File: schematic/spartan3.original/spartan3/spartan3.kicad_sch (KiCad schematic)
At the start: 206 parts, among them U1_clk_select_0 SPFT_Sliding_Switch-dynacore, U2 XC3S250E-4TQG144C

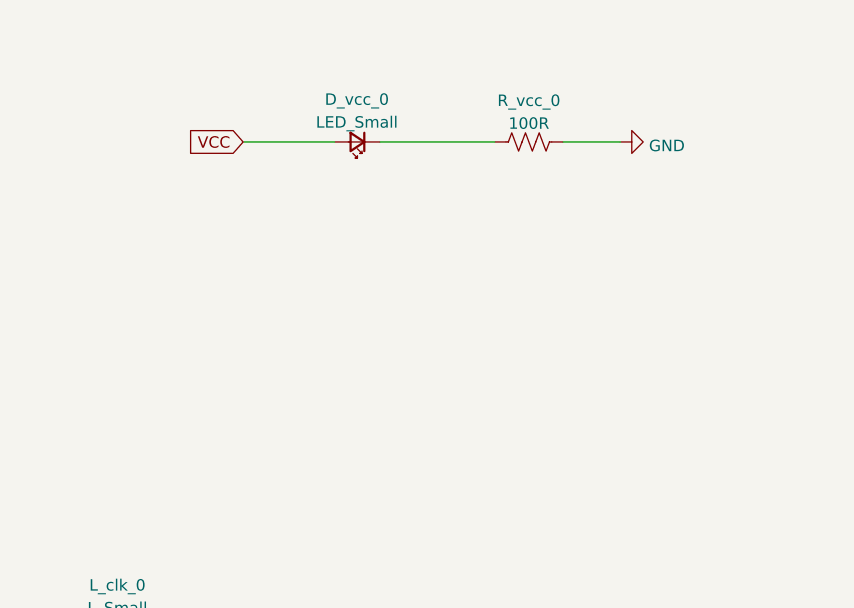
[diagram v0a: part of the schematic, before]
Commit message: Schematics :: reset added
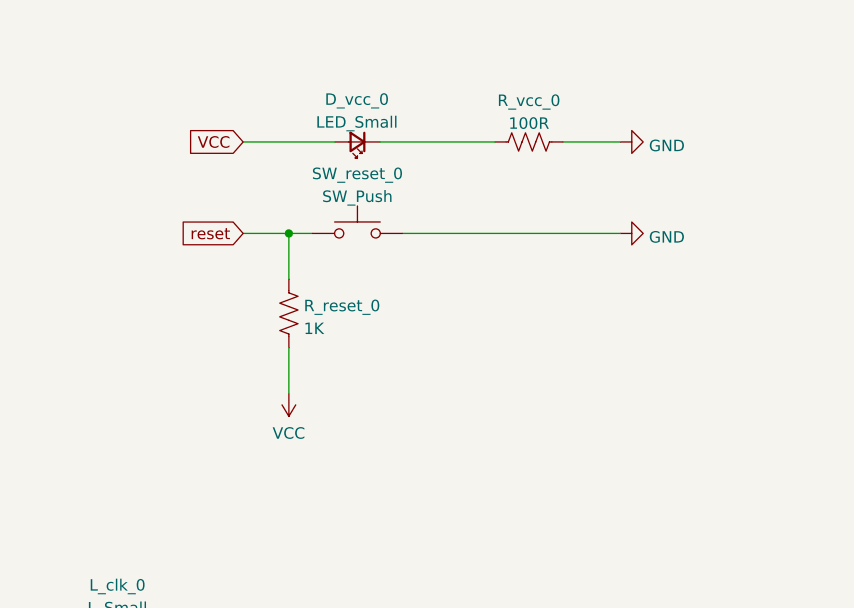
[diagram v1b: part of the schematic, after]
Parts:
- added R_reset_0: 1K, Resistor_SMD:R_0805_2012Metric_Pad1.20x1.40mm_HandSolder, symbol Device:R_US
- added SW_reset_0: SW_Push, Button_Switch_THT:SW_PUSH_6mm_H9.5mm, symbol Switch:SW_Push
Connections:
- net GND: now also SW_reset_0.2
- net VCC: now also R_reset_0.1
- new net reset: R_reset_0.2, SW_reset_0.1
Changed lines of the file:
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@@
   (junction (at 412.75 406.4) (diameter 0) (color 0 0 0 0)
   )
+  (junction (at 850.9 248.92) (diameter 0) (color 0 0 0 0)
+  )
   (junction (at 685.8 177.8) (diameter 0) (color 0 0 0 0)
   )
@@
     (stroke (width 0) (type default) (color 0 0 0 0))
   )
+  (wire (pts (xy 845.82 248.92) (xy 850.9 248.92))
+    (stroke (width 0) (type default) (color 0 0 0 0))
+  )
   (wire (pts (xy 412.75 298.45) (xy 412.75 299.72))
     (stroke (width 0) (type default) (color 0 0 0 0))
@@
     (stroke (width 0) (type default) (color 0 0 0 0))
   )
+  (wire (pts (xy 850.9 248.92) (xy 850.9 254))
+    (stroke (width 0) (type default) (color 0 0 0 0))
+  )
   (wire (pts (xy 317.5 297.18) (xy 317.5 298.45))
     (stroke (width 0) (type default) (color 0 0 0 0))
@@
     (stroke (width 0) (type default) (color 0 0 0 0))
   )
+  (wire (pts (xy 850.9 248.92) (xy 853.44 248.92))
+    (stroke (width 0) (type default) (color 0 0 0 0))
+  )
   (wire (pts (xy 901.7 309.88) (xy 914.4 309.88))
     (stroke (width 0) (type default) (color 0 0 0 0))
@@
     (stroke (width 0) (type default) (color 0 0 0 0))
   )
+  (wire (pts (xy 863.6 248.92) (xy 887.73 248.92))
+    (stroke (width 0) (type default) (color 0 0 0 0))
+  )
   (wire (pts (xy 129.54 215.9) (xy 139.7 215.9))
     (stroke (width 0) (type default) (color 0 0 0 0))
@@
     (stroke (width 0) (type default) (color 0 0 0 0))
   )
+  (wire (pts (xy 850.9 261.62) (xy 850.9 266.7))
+    (stroke (width 0) (type default) (color 0 0 0 0))
+  )
   (wire (pts (xy 508 50.8) (xy 514.35 50.8))
     (stroke (width 0) (type default) (color 0 0 0 0))
@@
     )
   )
+  (global_label "reset" (shape input) (at 845.82 248.92 180) (fields_autoplaced)
+    (effects (font (size 1.27 1.27)) (justify right))
+    (property "Intersheet References" "${INTERSHEET_REFS}" (id 0) (at 838.6898 248.8406 0)
+      (effects (font (size 1.27 1.27)) (justify right) hide)
+    )
+  )
   (global_label "in_ram_w" (shape input) (at 675.64 330.2 180) (fields_autoplaced)
     (effects (font (size 1.27 1.27)) (justify right))
@@
     (pin "1")
   )
+  (symbol (lib_id "Switch:SW_Push") (at 858.52 248.92 0) (unit 1)
+    (in_bom yes) (on_board yes) (fields_autoplaced)
+    (property "Reference" "SW_reset_0" (id 0) (at 858.52 242.2992 0))
+    (property "Value" "SW_Push" (id 1) (at 858.52 244.8361 0))
+    (property "Footprint" "Button_Switch_THT:SW_PUSH_6mm_H9.5mm" (id 2) (at 858.52 243.84 0)
+      (effects (font (size 1.27 1.27)) hide)
+    )
+    (property "Datasheet" "~" (id 3) (at 858.52 243.84 0)
+      (effects (font (size 1.27 1.27)) hide)
+    )
+    (pin "1")
+    (pin "2")
+  )
   (symbol (lib_id "Device:LED_Small") (at 762 173.99 90) (unit 1)
     (in_bom yes) (on_board yes) (fields_autoplaced)
@@
     (pin "1")
   )
+  (symbol (lib_id "power:VCC") (at 850.9 266.7 180) (unit 1)
+    (in_bom yes) (on_board yes) (fields_autoplaced)
+    (property "Reference" "#PWR0252" (id 0) (at 850.9 262.89 0)
+      (effects (font (size 1.27 1.27)) hide)
+    )
+    (property "Value" "VCC" (id 1) (at 850.9 271.1434 0))
+    (property "Footprint" "" (id 2) (at 850.9 266.7 0)
+      (effects (font (size 1.27 1.27)) hide)
+    )
+    (property "Datasheet" "" (id 3) (at 850.9 266.7 0)
+      (effects (font (size 1.27 1.27)) hide)
+    )
+    (pin "1")
+  )
   (symbol (lib_id "power:GND") (at 717.55 213.36 90) (unit 1)
     (in_bom yes) (on_board yes) (fields_autoplaced)
@@
     (pin "2")
   )
+  (symbol (lib_id "power:GND") (at 887.73 248.92 90) (unit 1)
+    (in_bom yes) (on_board yes) (fields_autoplaced)
+    (property "Reference" "#PWR0251" (id 0) (at 894.08 248.92 0)
+      (effects (font (size 1.27 1.27)) hide)
+    )
+    (property "Value" "GND" (id 1) (at 890.905 249.3538 90)
+      (effects (font (size 1.27 1.27)) (justify right))
+    )
+    (property "Footprint" "" (id 2) (at 887.73 248.92 0)
+      (effects (font (size 1.27 1.27)) hide)
+    )
+    (property "Datasheet" "" (id 3) (at 887.73 248.92 0)
+      (effects (font (size 1.27 1.27)) hide)
+    )
+    (pin "1")
+  )
   (symbol (lib_id "power:VCC") (at 514.35 76.2 180) (unit 1)
     (in_bom yes) (on_board yes) (fields_autoplaced)
@@
     (pin "2")
   )
+  (symbol (lib_id "Device:R_US") (at 850.9 257.81 180) (unit 1)
+    (in_bom yes) (on_board yes) (fields_autoplaced)
+    (property "Reference" "R_reset_0" (id 0) (at 852.551 256.9753 0)
+      (effects (font (size 1.27 1.27)) (justify right))
+    )
+    (property "Value" "1K" (id 1) (at 852.551 259.5122 0)
+      (effects (font (size 1.27 1.27)) (justify right))
+    )
+    (property "Footprint" "Resistor_SMD:R_0805_2012Metric_Pad1.20x1.40mm_HandSolder" (id 2) (at 849.884 257.556 90)
+      (effects (font (size 1.27 1.27)) hide)
+    )
+    (property "Datasheet" "~" (id 3) (at 850.9 257.81 0)
+      (effects (font (size 1.27 1.27)) hide)
+    )
+    (pin "1")
+    (pin "2")
+  )
   (symbol (lib_id "Device:R_US") (at 450.85 67.31 0) (unit 1)
     (in_bom yes) (on_board yes) (fields_autoplaced)
@@
       (reference "#PWR0250") (unit 1) (value "GND") (footprint "")
     )
+    (path "/c2e867b7-cc1c-4161-9b5f-6d9bb039bb16"
+      (reference "#PWR0251") (unit 1) (value "GND") (footprint "")
+    )
+    (path "/c1058ec3-aaf6-4e15-be2c-ea2cca1c2665"
+      (reference "#PWR0252") (unit 1) (value "VCC") (footprint "")
+    )
     (path "/25f84511-8044-4092-a57a-275fe021ef47"
       (reference "C_clk_0") (unit 1) (value "0.1uF") (footprint "Capacitor_SMD:C_0805_2012Metric_Pad1.18x1.45mm_HandSolder")
@@
       (reference "R_out_temp_w_0") (unit 1) (value "100R") (footprint "Resistor_SMD:R_0805_2012Metric_Pad1.20x1.40mm_HandSolder")
     )
+    (path "/fc10d999-524c-4ab3-9f2d-33fffce35e4f"
+      (reference "R_reset_0") (unit 1) (value "1K") (footprint "Resistor_SMD:R_0805_2012Metric_Pad1.20x1.40mm_HandSolder")
+    )
     (path "/37f06184-9457-42c5-a75e-4071dfdcb627"
       (reference "R_vcc_0") (unit 1) (value "100R") (footprint "Resistor_SMD:R_0805_2012Metric_Pad1.20x1.40mm_HandSolder")
@@
       (reference "SW_read_register_0") (unit 1) (value "SW_Rotary12") (footprint "SR26 1-1-12P:SR26 1-1-12P")
     )
+    (path "/1682c353-3a8a-416c-8478-fd455b67bc33"
+      (reference "SW_reset_0") (unit 1) (value "SW_Push") (footprint "Button_Switch_THT:SW_PUSH_6mm_H9.5mm")
+    )
     (path "/3dc17902-13b6-4e7e-8b7b-bbfdc1838232"

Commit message: PCB layout :: Implementation process started
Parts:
- D_out_sysbus_0, D_out_sysbus_1, D_out_sysbus_2, D_out_sysbus_3, D_out_sysbus_4, D_out_sysbus_5, D_out_sysbus_6, D_out_sysbus_7: footprint SW_SPDT_small:SW_SPDT_Small -> LED_SMD:LED_0805_2012Metric_Pad1.15x1.40mm_HandSolder
- SW_in_manual_input_o_0, SW_in_manual_input_o_1, SW_in_manual_input_o_2, SW_in_manual_input_o_3, SW_in_manual_input_o_4, SW_in_manual_input_o_5, SW_in_manual_input_o_6, SW_in_manual_input_o_7: footprint Button_Switch_THT:SW_Slide_1P2T_CK_OS102011MS2Q -> SW_SPDT_small:SW_SPDT_Small
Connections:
- net GND: now also U1_clk_select_0.1 (Common), U1_clk_select_0.7 (Common); no longer U1_clk_select_0.~ (P5)
- net in_is_clk_external: now also U1_clk_select_0.3 (P2); no longer U1_clk_select_0.~ (P5)
- net in_is_clk_high: now also U1_clk_select_0.4 (P3); no longer U1_clk_select_0.~ (P5)
- net in_is_clk_low: now also U1_clk_select_0.5 (P4); no longer U1_clk_select_0.~ (P5)
- net in_is_clk_manual: now also U1_clk_select_0.6 (P5); no longer U1_clk_select_0.~ (P5)
- net in_is_clk_veryhigh: now also U1_clk_select_0.2 (P1); no longer U1_clk_select_0.~ (P5)

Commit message: Schematics :: Read Register fixed -- Rs added. PCB layout :: Updated
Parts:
- added D_in_none_r_0: LED_Small, LED_SMD:LED_0805_2012Metric_Pad1.15x1.40mm_HandSolder, symbol Device:LED_Small
- added R_d_in_acc_r_0, R_d_in_iar_r_0, R_d_in_ir_r_0, R_d_in_manual_input_r_0, R_d_in_none_r_0, R_d_in_r0_r_0, R_d_in_r1_r_0, R_d_in_r2_r_0, R_d_in_r3_r_0, R_d_in_ram_r_0: 100R, Resistor_SMD:R_0805_2012Metric_Pad1.20x1.40mm_HandSolder, symbol Device:R_US
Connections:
- net VCC: now also R_d_in_acc_r_0.1, R_d_in_iar_r_0.1, R_d_in_ir_r_0.1, R_d_in_manual_input_r_0.1, R_d_in_none_r_0.1, R_d_in_r0_r_0.1, R_d_in_r1_r_0.1, R_d_in_r2_r_0.1, R_d_in_r3_r_0.1, R_d_in_ram_r_0.1; no longer D_in_acc_r_0.2 (A), D_in_iar_r_0.2 (A), D_in_ir_r_0.2 (A), D_in_manual_input_r_0.2 (A), D_in_r0_r_0.2 (A), D_in_r1_r_0.2 (A), D_in_r2_r_0.2 (A), D_in_r3_r_0.2 (A), D_in_ram_r_0.2 (A)
- net in_acc_r: now also SW_read_register_0.7; no longer SW_read_register_0.3
- net in_iar_r: now also SW_read_register_0.5; no longer SW_read_register_0.1
- net in_ir_r: now also SW_read_register_0.6; no longer SW_read_register_0.2
- net in_manual_input_r: now also SW_read_register_0.1; no longer SW_read_register_0.9
- net in_r0_r: now also SW_read_register_0.9; no longer SW_read_register_0.5
- net in_r1_r: now also SW_read_register_0.10; no longer SW_read_register_0.6
- net in_r2_r: now also SW_read_register_0.11; no longer SW_read_register_0.7
- net in_r3_r: now also SW_read_register_0.12; no longer SW_read_register_0.8
- net in_ram_r: now also SW_read_register_0.8; no longer SW_read_register_0.4
- new net: D_in_none_r_0.1 (K), SW_read_register_0.4
- new net: D_in_manual_input_r_0.2 (A), R_d_in_manual_input_r_0.2
- new net: D_in_iar_r_0.2 (A), R_d_in_iar_r_0.2
- new net: D_in_acc_r_0.2 (A), R_d_in_acc_r_0.2
- new net: D_in_r0_r_0.2 (A), R_d_in_r0_r_0.2
- new net: D_in_r3_r_0.2 (A), R_d_in_r3_r_0.2
- new net: D_in_r1_r_0.2 (A), R_d_in_r1_r_0.2
- new net: D_in_ram_r_0.2 (A), R_d_in_ram_r_0.2
- new net: D_in_r2_r_0.2 (A), R_d_in_r2_r_0.2
- new net: D_in_ir_r_0.2 (A), R_d_in_ir_r_0.2
- new net: D_in_none_r_0.2 (A), R_d_in_none_r_0.2
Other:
- moved on the sheet: D_in_acc_r_0, D_in_iar_r_0, D_in_ir_r_0, D_in_manual_input_r_0, D_in_r0_r_0, D_in_r1_r_0, D_in_r2_r_0, D_in_r3_r_0, D_in_ram_r_0, R_in_acc_r_0, R_in_iar_r_0, R_in_ir_r_0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

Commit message: Schematics :: updated / PCB layout :: updated
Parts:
- added R_d_in_acc_w_0, R_d_in_bus1_one_0, R_d_in_bus1_ps_0, R_d_in_clk_manual_0, R_d_in_iar_w_0, R_d_in_ir_w_0, R_d_in_is_bus1_w_0, R_d_in_is_clk_external_0, R_d_in_is_clk_high_0, R_d_in_is_clk_low_0, R_d_in_is_clk_manual_0, R_d_in_is_clk_veryhigh_0, R_d_in_r0_w_0, R_d_in_r1_w_0, R_d_in_r2_w_0, R_d_in_r3_w_0, R_d_in_ram_a_w_0, R_d_in_ram_w_0, R_d_in_read_reg_en_0, R_d_in_temp_w_0, R_d_in_write_reg_en_0: 100R, Resistor_SMD:R_0805_2012Metric_Pad1.20x1.40mm_HandSolder, symbol Device:R_US
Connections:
- net GND: now also R_d_in_bus1_ps_0.1; no longer D_in_bus1_ps_0.1 (K)
- net VCC: now also R_d_in_acc_w_0.1, R_d_in_bus1_one_0.2, R_d_in_clk_manual_0.1, R_d_in_iar_w_0.1, R_d_in_ir_w_0.1, R_d_in_is_bus1_w_0.1, R_d_in_is_clk_external_0.1, R_d_in_is_clk_high_0.1, R_d_in_is_clk_low_0.1, R_d_in_is_clk_manual_0.1, R_d_in_is_clk_veryhigh_0.1, R_d_in_r0_w_0.1, R_d_in_r1_w_0.1, R_d_in_r2_w_0.1, R_d_in_r3_w_0.1, R_d_in_ram_a_w_0.1, R_d_in_ram_w_0.1, R_d_in_read_reg_en_0.1, R_d_in_temp_w_0.1, R_d_in_write_reg_en_0.1; no longer D_in_acc_w_0.2 (A), D_in_bus1_one_0.2 (A), D_in_clk_manual_0.2 (A), D_in_iar_w_0.2 (A), D_in_ir_w_0.2 (A), D_in_is_bus1_w_0.2 (A), D_in_is_clk_external_0.2 (A), D_in_is_clk_high_0.2 (A), D_in_is_clk_low_0.2 (A), D_in_is_clk_manual_0.2 (A), D_in_is_clk_veryhigh_0.2 (A), D_in_r0_w_0.2 (A), D_in_r1_w_0.2 (A), D_in_r2_w_0.2 (A), D_in_r3_w_0.2 (A), D_in_ram_a_w_0.2 (A), D_in_ram_w_0.2 (A), D_in_read_reg_en_0.2 (A), D_in_temp_w_0.2 (A), D_in_write_reg_en_0.2 (A)
- new net: D_in_is_clk_external_0.2 (A), R_d_in_is_clk_external_0.2
- new net: D_in_bus1_one_0.2 (A), R_d_in_bus1_one_0.1
- new net: D_in_is_bus1_w_0.2 (A), R_d_in_is_bus1_w_0.2
- new net: D_in_r2_w_0.2 (A), R_d_in_r2_w_0.2
- new net: D_in_temp_w_0.2 (A), R_d_in_temp_w_0.2
- new net: D_in_r1_w_0.2 (A), R_d_in_r1_w_0.2
- new net: D_in_ram_w_0.2 (A), R_d_in_ram_w_0.2
- new net: D_in_ram_a_w_0.2 (A), R_d_in_ram_a_w_0.2
- new net: D_in_r0_w_0.2 (A), R_d_in_r0_w_0.2
- new net: D_in_acc_w_0.2 (A), R_d_in_acc_w_0.2
- new net: D_in_r3_w_0.2 (A), R_d_in_r3_w_0.2
- new net: D_in_ir_w_0.2 (A), R_d_in_ir_w_0.2
- new net: D_in_clk_manual_0.2 (A), R_d_in_clk_manual_0.2
- new net: D_in_read_reg_en_0.2 (A), R_d_in_read_reg_en_0.2
- new net: D_in_is_clk_veryhigh_0.2 (A), R_d_in_is_clk_veryhigh_0.2
- new net: D_in_write_reg_en_0.2 (A), R_d_in_write_reg_en_0.2
- new net: D_in_iar_w_0.2 (A), R_d_in_iar_w_0.2
- new net: D_in_is_clk_high_0.2 (A), R_d_in_is_clk_high_0.2
- new net: D_in_bus1_ps_0.1 (K), R_d_in_bus1_ps_0.2
- new net: D_in_is_clk_low_0.2 (A), R_d_in_is_clk_low_0.2
- new net: D_in_is_clk_manual_0.2 (A), R_d_in_is_clk_manual_0.2
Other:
- moved on the sheet: D_in_bus1_one_0, D_in_bus1_ps_0, D_in_r0_w_0, D_in_r1_w_0, D_in_r2_w_0, D_in_r3_w_0, D_in_temp_w_0, R_in_bus1_0, R_in_r0_w_0, R_in_r1_w_0, R_in_r2_w_0, R_in_r3_w_0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

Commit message: Schematic :: LED R/SW_DPDT updated. PCB layout :: logic, non FPGA connections implemented
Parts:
- removed SW_in_acc_w_0, SW_in_iar_w_0, SW_in_ir_w_0, SW_in_r0_w_0, SW_in_r1_w_0, SW_in_r2_w_0, SW_in_r3_w_0, SW_in_ram_a_w_0, SW_in_ram_w_0, SW_in_temp_w_0: SW_DPDT_x2, Button_Switch_THT:SW_Push_2P2T_Toggle_CK_PVA2OAH5xxxxxxV2, symbol Switch:SW_DPDT_x2
- added SW_in_acc_w_0, SW_in_iar_w_0, SW_in_ir_w_0, SW_in_r0_w_0, SW_in_r1_w_0, SW_in_r2_w_0, SW_in_r3_w_0, SW_in_ram_a_w_0, SW_in_ram_w_0, SW_in_temp_w_0: SW_DPDT_x2, Button_Switch_THT:SW_Push_2P2T_Toggle_CK_PVA2OAH5xxxxxxV2, symbol Switch:SW_DPDT_x2
- R_d_in_acc_r_0, R_d_in_acc_w_0, R_d_in_bus1_one_0, R_d_in_bus1_ps_0, R_d_in_clk_manual_0, R_d_in_iar_r_0, R_d_in_iar_w_0, R_d_in_ir_r_0, R_d_in_ir_w_0, R_d_in_is_bus1_w_0, R_d_in_is_clk_external_0, R_d_in_is_clk_high_0, R_d_in_is_clk_low_0, R_d_in_is_clk_manual_0, R_d_in_is_clk_veryhigh_0, R_d_in_manual_input_r_0, R_d_in_none_r_0, R_d_in_r0_r_0, R_d_in_r0_w_0, R_d_in_r1_r_0, R_d_in_r1_w_0, R_d_in_r2_r_0, R_d_in_r2_w_0, R_d_in_r3_r_0, R_d_in_r3_w_0, R_d_in_ram_a_w_0, R_d_in_ram_r_0, R_d_in_ram_w_0, R_d_in_read_reg_en_0, R_d_in_temp_w_0, R_d_in_write_reg_en_0, R_out_acc_r_0, R_out_acc_w_0, R_out_bus1_0, R_out_can_read_0, R_out_can_write_0, R_out_clk_internal_0, R_out_clkc_0, R_out_clkr_0, R_out_clkw_0, R_out_flags_C_out_0, R_out_flags_eq_0, R_out_flags_gt_0, R_out_flags_w_0, R_out_flags_z_0, R_out_iar_r_0, R_out_iar_w_0, R_out_ir_w_0, R_out_is_bus1_w_0, R_out_r0_r_0, R_out_r0_w_0, R_out_r1_r_0, R_out_r1_w_0, R_out_r2_r_0, R_out_r2_w_0, R_out_r3_r_0, R_out_r3_w_0, R_out_ram_a_w_0, R_out_ram_r_0, R_out_ram_w_0, R_out_s1_0, R_out_s2_0, R_out_s3_0, R_out_s4_0, R_out_s5_0, R_out_s6_0, R_out_sysbus_0, R_out_sysbus_1, R_out_sysbus_2, R_out_sysbus_3, R_out_sysbus_4, R_out_sysbus_5, R_out_sysbus_6, R_out_sysbus_7, R_out_temp_w_0, R_vcc_0: value 100R -> 68R
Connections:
- net GND: now also SW_in_acc_w_0.4 (A), SW_in_iar_w_0.4 (A), SW_in_ir_w_0.4 (A), SW_in_r0_w_0.4 (A), SW_in_r1_w_0.4 (A), SW_in_r2_w_0.4 (A), SW_in_r3_w_0.4 (A), SW_in_ram_a_w_0.4 (A), SW_in_ram_w_0.4 (A), SW_in_temp_w_0.4 (A)
- net in_acc_w: now also SW_in_acc_w_0.5 (B)
- net in_iar_w: now also SW_in_iar_w_0.5 (B)
- net in_ir_w: now also SW_in_ir_w_0.5 (B)
- net in_r0_w: now also SW_in_r0_w_0.5 (B)
- net in_r1_w: now also SW_in_r1_w_0.5 (B)
- net in_r2_w: now also SW_in_r2_w_0.5 (B)
- net in_r3_w: now also SW_in_r3_w_0.5 (B)
- net in_ram_a_w: now also SW_in_ram_a_w_0.5 (B)
- net in_ram_w: now also SW_in_ram_w_0.5 (B)
- net in_temp_w: now also SW_in_temp_w_0.5 (B)

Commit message: Schematics :: J_CONTROL added. PCB layout :: updated
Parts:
- added J_CONTROL_0: Conn_01x25_Male, Connector_PinHeader_2.54mm:PinHeader_1x25_P2.54mm_Vertical, symbol Connector:Conn_01x25_Male
- added J_FPGA_B_0, J_FPGA_B_1, J_FPGA_B_2, J_FPGA_B_3: Conn_01x36_Male, Connector_PinHeader_2.54mm:PinHeader_1x36_P2.54mm_Vertical, symbol Connector:Conn_01x36_Male
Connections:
- net GND: now also J_CONTROL_0.4 (Pin_4), J_FPGA_B_0.10 (Pin_10), J_FPGA_B_0.19 (Pin_19), J_FPGA_B_0.25 (Pin_25), J_FPGA_B_1.1 (Pin_1), J_FPGA_B_1.18 (Pin_18), J_FPGA_B_1.27 (Pin_27), J_FPGA_B_2.1 (Pin_1), J_FPGA_B_2.10 (Pin_10), J_FPGA_B_2.19 (Pin_19), J_FPGA_B_2.25 (Pin_25), J_FPGA_B_3.11 (Pin_11), J_FPGA_B_3.19 (Pin_19), J_FPGA_B_3.27 (Pin_27)
- net VCC: now also J_CONTROL_0.1 (Pin_1)
- net VCC_banks: now also J_CONTROL_0.2 (Pin_2), J_FPGA_B_0.13 (Pin_13), J_FPGA_B_1.28 (Pin_28), J_FPGA_B_1.30 (Pin_30), J_FPGA_B_1.7 (Pin_7), J_FPGA_B_2.13 (Pin_13), J_FPGA_B_2.28 (Pin_28), J_FPGA_B_2.29 (Pin_29), J_FPGA_B_2.6 (Pin_6), J_FPGA_B_3.13 (Pin_13), J_FPGA_B_3.28 (Pin_28), J_FPGA_B_3.30 (Pin_30)
- net P110: now reaches R_JTAG_TCK_0.2, U2.110 (TCK)
- net P110: now also J_CONTROL_0.11 (Pin_11), J_FPGA_B_0.2 (Pin_2)
- net P10: now reaches U2.10 (IO_11_3)
- net P10: now also J_FPGA_B_3.10 (Pin_10)
- net P101: now reaches U2.101 (IP_4_1)
- net P101: now also J_FPGA_B_1.29 (Pin_29)
- net P103: now reaches U2.103 (IO_L09P_1)
- net P103: now also J_FPGA_B_1.31 (Pin_31)
- net P104: now reaches U2.104 (IO_L09N_1)
- net P104: now also J_FPGA_B_1.32 (Pin_32)
- net P105: now reaches U2.105 (IO_L10P_1)
- net P105: now also J_FPGA_B_1.33 (Pin_33)
- net P106: now reaches U2.106 (IO_L10N_1)
- net P106: now also J_FPGA_B_1.34 (Pin_34)
- net P107: now reaches U2.107 (IP_5_1)
- net P107: now also J_FPGA_B_1.35 (Pin_35)
- net P111: now reaches U2.111 (IP_1_0)
- net P111: now also J_FPGA_B_0.3 (Pin_3)
- net P112: now reaches U2.112 (IO_L01P_0)
- net P112: now also J_FPGA_B_0.4 (Pin_4)
- net P113: now reaches U2.113 (IO_L01N_0)
- net P113: now also J_FPGA_B_0.5 (Pin_5)
- net P114: now reaches U2.114 (IP_2_0)
- net P114: now also J_FPGA_B_0.6 (Pin_6)
- net P116: now reaches U2.116 (IO_L02P_0)
- net P116: now also J_FPGA_B_0.8 (Pin_8)
- net P117: now reaches U2.117 (IO_L02N_0)
- net P117: now also J_FPGA_B_0.9 (Pin_9)
- net P119: now reaches U2.119 (IP_L03P_0)
- net P119: now also J_FPGA_B_0.11 (Pin_11)
- net P12: now reaches U2.12 (IP_6_3_VREF)
- net P12: now also J_FPGA_B_3.12 (Pin_12)
- net P120: now reaches U2.120 (IP_L03N_0)
- net P120: now also J_FPGA_B_0.12 (Pin_12)
- net P122: now reaches U2.122 (IO_L04P_0_GCLK4)
- net P122: now also J_FPGA_B_0.14 (Pin_14)
- net P123: now reaches U2.123 (IO_L04N_0_GCLK5)
- net P123: now also J_FPGA_B_0.15 (Pin_15)
- net P124: now reaches U2.124 (IO_2_0_VREF)
- net P124: now also J_FPGA_B_0.16 (Pin_16)
- net P125: now reaches U2.125 (IO_L05P_0_GCLK6)
- net P125: now also J_FPGA_B_0.17 (Pin_17)
- net P126: now reaches U2.126 (IO_L05N_0_GCLK7)
- net P126: now also J_FPGA_B_0.18 (Pin_18)
- net P128: now reaches U2.128 (IP_L06P_0_GCLK8)
- net P128: now also J_FPGA_B_0.20 (Pin_20)
- net P129: now reaches U2.129 (IP_L06N_0_GCLK9)
- net P129: now also J_FPGA_B_0.21 (Pin_21)
- net P130: now reaches U2.130 (IO_L07P_0_GCLK10)
- net P130: now also J_FPGA_B_0.22 (Pin_22)
- net P131: now reaches U2.131 (IO_L07N_0_GCLK11)
- net P131: now also J_FPGA_B_0.23 (Pin_23)
- net P132: now reaches U2.132 (IO_1_0)
- net P132: now also J_FPGA_B_0.24 (Pin_24)
- net P134: now reaches U2.134 (IO_L08P_0)
- net P134: now also J_FPGA_B_0.26 (Pin_26)
- net P135: now reaches U2.135 (IO_L08N_0_VREF_0)
- net P135: now also J_FPGA_B_0.27 (Pin_27)
- net P136: now reaches U2.136 (IP_3_0)
- net P136: now also J_FPGA_B_0.28 (Pin_28)
- net P139: now reaches U2.139 (IO_L09P_0)
- net P139: now also J_FPGA_B_0.31 (Pin_31)
- net P14: now reaches U2.14 (IO_L04P_3_LHCLK0)
- net P14: now also J_FPGA_B_3.14 (Pin_14)
- net P140: now reaches U2.140 (IO_L09N_0)
- net P140: now also J_FPGA_B_0.32 (Pin_32)
- net P141: now reaches U2.141 (IP_4_0)
- net P141: now also J_FPGA_B_0.33 (Pin_33)
- net P142: now reaches U2.142 (IO_L10P_0)
- net P142: now also J_FPGA_B_0.34 (Pin_34)
- net P15: now reaches U2.15 (IO_L04N_3_LHCLK1)
- net P15: now also J_FPGA_B_3.15 (Pin_15)
- net P16: now reaches U2.16 (IO_L05P_3_LHCLK2)
- net P16: now also J_FPGA_B_3.16 (Pin_16)
- net P17: now reaches U2.17 (IO_L05N_3_LHCLK3)
- net P17: now also J_FPGA_B_3.17 (Pin_17)
- net P18: now reaches U2.18 (IP_3_3)
- net P18: now also J_FPGA_B_3.18 (Pin_18)
- net P2: now reaches U2.2 (IO_L01P_3)
- net P2: now also J_FPGA_B_3.2 (Pin_2)
- net P20: now reaches U2.20 (IO_L06P_3_LHCLK4)
- net P20: now also J_FPGA_B_3.20 (Pin_20)
- net P21: now reaches U2.21 (IO_L06N_3_LHCLK5)
- net P21: now also J_FPGA_B_3.21 (Pin_21)
- net P22: now reaches U2.22 (IO_L07P_3_LHCLK6)
- net P22: now also J_FPGA_B_3.22 (Pin_22)
- net P23: now reaches U2.23 (IO_L07N_3_LHCLK7)
- net P23: now also J_FPGA_B_3.23 (Pin_23)
- net P24: now reaches U2.24 (IP_4_3)
- net P24: now also J_FPGA_B_3.24 (Pin_24)
- net P25: now reaches U2.25 (IO_L08P_3)
- net P25: now also J_FPGA_B_3.25 (Pin_25)
- net P26: now reaches U2.26 (IO_L08N_3)
- net P26: now also J_FPGA_B_3.26 (Pin_26)
- net P29: now reaches U2.29 (IO_12_3)
- net P29: now also J_FPGA_B_3.29 (Pin_29)
- net P3: now reaches U2.3 (IO_L01N_3)
- net P3: now also J_FPGA_B_3.3 (Pin_3)
- net P31: now reaches U2.31 (IP_1_3_VREF)
- net P31: now also J_FPGA_B_3.31 (Pin_31)
- net P32: now reaches U2.32 (IO_L09P_3)
- net P32: now also J_FPGA_B_3.32 (Pin_32)
- net P33: now reaches U2.33 (IO_L09N_3)
- net P33: now also J_FPGA_B_3.33 (Pin_33)
- net P34: now reaches U2.34 (IO_L10P_3)
- net P34: now also J_FPGA_B_3.34 (Pin_34)
- net P35: now reaches U2.35 (IO_L10N_3)
- net P35: now also J_FPGA_B_3.35 (Pin_35)
- net P36: now reaches U2.36 (IP_5_3)
- net P36: now also J_FPGA_B_3.36 (Pin_36)
- net P38: now reaches U2.38 (IP_2_2)
- net P38: now also J_FPGA_B_2.2 (Pin_2)
- net P4: now reaches U2.4 (IO_L02P_3)
- net P4: now also J_FPGA_B_3.4 (Pin_4)
- net P41: now reaches U2.41 (IP_3_2)
- net P41: now also J_FPGA_B_2.5 (Pin_5)
- net P47: now reaches U2.47 (IP_L03P_2)
- net P47: now also J_FPGA_B_2.11 (Pin_11)
- net P48: now reaches U2.48 (IP_L03N_2_VREF_2)
- net P48: now also J_FPGA_B_2.12 (Pin_12)
- net P5: now reaches U2.5 (IO_L02N_3_VREF)
- net P5: now also J_FPGA_B_3.5 (Pin_5)
- net P50: now reaches U2.50 (IO_L04P_2_GCLK12)
- net P50: now also J_FPGA_B_2.14 (Pin_14)
- net P51: now reaches U2.51 (IO_L04N_2_GCLK13)
- net P51: now also J_FPGA_B_2.15 (Pin_15)
- net P52: now reaches U2.52 (IO_1_2)
- net P52: now also J_FPGA_B_2.16 (Pin_16)
- net P53: now reaches U2.53 (IO_L05P_2_GCLK14)
- net P53: now also J_FPGA_B_2.17 (Pin_17)
- net P54: now reaches U2.54 (IO_L05N_2_GCLK15)
- net P54: now also J_FPGA_B_2.18 (Pin_18)
- net P58: now reaches U2.58 (IO_L07P_2_GCLK2)
- net P58: now also J_FPGA_B_2.22 (Pin_22)
- net P59: now reaches U2.59 (IO_L07N_2_GCLK3)
- net P59: now also J_FPGA_B_2.23 (Pin_23)
- net P6: now reaches U2.6 (IP_2_3)
- net P6: now also J_FPGA_B_3.6 (Pin_6)
- net P66: now reaches U2.66 (IP_1_2_VREF)
- net P66: now also J_FPGA_B_2.30 (Pin_30)
- net P67: now reaches U2.67 (IO_L09P_2_VS2)
- net P67: now also J_FPGA_B_2.31 (Pin_31)
- net P68: now reaches U2.68 (IO_L09N_2_VS1)
- net P68: now also J_FPGA_B_2.32 (Pin_32)
- net P69: now reaches U2.69 (IP_4_2)
- net P69: now also J_FPGA_B_2.33 (Pin_33)
- net P7: now reaches U2.7 (IO_L03P_3)
- net P7: now also J_FPGA_B_3.7 (Pin_7)
- net P70: now reaches U2.70 (IO_L10P_2_VS0)
- net P70: now also J_FPGA_B_2.34 (Pin_34)
- net P74: now reaches U2.74 (IO_L01P_1)
- net P74: now also J_FPGA_B_1.2 (Pin_2)
- net P75: now reaches U2.75 (IO_L01N_1)
- net P75: now also J_FPGA_B_1.3 (Pin_3)
- net P76: now reaches U2.76 (IO_L02P_1)
- net P76: now also J_FPGA_B_1.4 (Pin_4)
- net P77: now reaches U2.77 (IO_L02N_1)
- net P77: now also J_FPGA_B_1.5 (Pin_5)
- net P78: now reaches U2.78 (IP_1_1)
- net P78: now also J_FPGA_B_1.6 (Pin_6)
- net P8: now reaches U2.8 (IO_L03N_3)
- net P8: now also J_FPGA_B_3.8 (Pin_8)
- net P81: now reaches U2.81 (IO_L03P_1)
- net P81: now also J_FPGA_B_1.9 (Pin_9)
- net P82: now reaches U2.82 (IO_L03N_1)
- net P82: now also J_FPGA_B_1.10 (Pin_10)
- net P83: now reaches U2.83 (IO_2_1_VREF)
- net P83: now also J_FPGA_B_1.11 (Pin_11)
- net P84: now reaches U2.84 (IP_2_1)
- net P84: now also J_FPGA_B_1.12 (Pin_12)
- net P85: now reaches U2.85 (IO_L04P_1_RHCLK0)
- net P85: now also J_FPGA_B_1.13 (Pin_13)
- net P86: now reaches U2.86 (IO_L04N_1_RHCLK1)
- net P86: now also J_FPGA_B_1.14 (Pin_14)
- net P87: now reaches U2.87 (IO_L05P_1_RHCLK2)
- net P87: now also J_FPGA_B_1.15 (Pin_15)
- net P88: now reaches U2.88 (IO_L05N_1_RHCLK3)
- net P88: now also J_FPGA_B_1.16 (Pin_16)
- net P89: now reaches U2.89 (IP_3_1)
- net P89: now also J_FPGA_B_1.17 (Pin_17)
- net P91: now reaches U2.91 (IO_L06P_1_RHCLK4)
- net P91: now also J_FPGA_B_1.19 (Pin_19)
- net P92: now reaches U2.92 (IO_L06N_1_RHCLK5)
- net P92: now also J_FPGA_B_1.20 (Pin_20)
- net P93: now reaches U2.93 (IO_L07P_1_RHCLK6)
- net P93: now also J_FPGA_B_1.21 (Pin_21)
- net P94: now reaches U2.94 (IO_L07N_1_RHCLK7)
- net P94: now also J_FPGA_B_1.22 (Pin_22)
- net P95: now reaches U2.95 (IP_6_1_VREF)
- net P95: now also J_FPGA_B_1.23 (Pin_23)
- net P96: now reaches U2.96 (IO_L08P_1)
- net P96: now also J_FPGA_B_1.24 (Pin_24)
- net P97: now reaches U2.97 (IO_L08N_1)
- net P97: now also J_FPGA_B_1.25 (Pin_25)
- net P98: now reaches U2.98 (IO_1_1)
- net P98: now also J_FPGA_B_1.26 (Pin_26)
- net VCC_core: now reaches U2.115 (VCCINT4), U2.45 (VCCINT2), U2.80 (VCCINT3), U2.9 (VCCINT1), U_pwr_vcc_core_0.2 (VO)
- net VCC_core: now also J_CONTROL_0.3 (Pin_3), J_FPGA_B_0.7 (Pin_7), J_FPGA_B_1.8 (Pin_8), J_FPGA_B_2.9 (Pin_9), J_FPGA_B_3.9 (Pin_9)
- net P1: now reaches U2.1 (PROG_B)
- net P1: now also J_CONTROL_0.9 (Pin_9), J_FPGA_B_3.1 (Pin_1)
- net P108: now reaches R_JTAG_TMS_0.2, U2.108 (TMS)
- net P108: now also J_CONTROL_0.12 (Pin_12), J_FPGA_B_1.36 (Pin_36)
- net P109: now reaches R_JTAG_TDO_0.2, U2.109 (TDO)
- net P109: now also J_CONTROL_0.14 (Pin_14), J_FPGA_B_0.1 (Pin_1)
- net HSWAP_EN: now reaches U2.143 (HSWAP_EN)
- net HSWAP_EN: now also J_CONTROL_0.18 (Pin_18), J_FPGA_B_0.35 (Pin_35)
- net P144: now reaches R_JTAG_TDI_0.2, U2.144 (TDI)
- net P144: now also J_CONTROL_0.13 (Pin_13), J_FPGA_B_0.36 (Pin_36)
- net INIT_B: now reaches U2.40 (INIT_B)
- net INIT_B: now also J_CONTROL_0.10 (Pin_10), J_FPGA_B_2.4 (Pin_4)
- net DOUT_BUSY: now reaches U2.43 (DOUT_BUSY)
- net DOUT_BUSY: now also J_CONTROL_0.7 (Pin_7), J_FPGA_B_2.7 (Pin_7)
- net M2: now reaches U2.57 (M2)
- net M2: now also J_CONTROL_0.15 (Pin_15), J_FPGA_B_2.21 (Pin_21)
- net M1: now reaches U2.60 (M1)
- net M1: now also J_CONTROL_0.16 (Pin_16), J_FPGA_B_2.24 (Pin_24)
- net M0: now reaches U2.62 (M0)
- net M0: now also J_CONTROL_0.17 (Pin_17), J_FPGA_B_2.26 (Pin_26)
- net DONE: now reaches U2.72 (DONE)
- net DONE: now also J_CONTROL_0.8 (Pin_8), J_FPGA_B_2.36 (Pin_36)
- net clk renamed P56
- net P56: now also J_CONTROL_0.23 (Pin_23), J_FPGA_B_2.20 (Pin_20)
- net eeprom_spi_clk renamed CCLK
- net CCLK: now also J_CONTROL_0.22 (Pin_22), J_CONTROL_0.5 (Pin_5), J_FPGA_B_2.35 (Pin_35)
- net eeprom_spi_dout renamed D0_DIN
- net D0_DIN: now also J_CONTROL_0.21 (Pin_21), J_CONTROL_0.6 (Pin_6), J_FPGA_B_2.27 (Pin_27)
- net eprom_spi_cs_n renamed P39
- net P39: now also J_CONTROL_0.19 (Pin_19), J_FPGA_B_2.3 (Pin_3)
- net eprom_spi_din renamed P44
- net P44: now also J_CONTROL_0.20 (Pin_20), J_FPGA_B_2.8 (Pin_8)
- new net P137: J_FPGA_B_0.29 (Pin_29)
- new net P138: J_FPGA_B_0.30 (Pin_30)
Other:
- moved on the sheet: P_JTAG_0, R_JTAG_TCK_0, R_JTAG_TDI_0, R_JTAG_TDO_0, R_JTAG_TMS_0
